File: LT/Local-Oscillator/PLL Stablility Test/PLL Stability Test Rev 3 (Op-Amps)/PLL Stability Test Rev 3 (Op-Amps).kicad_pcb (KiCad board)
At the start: 2 copper layers, 30 parts, among them J1 Conn_01x02_Male, J10 Conn_01x02_Male, J2 Conn_Coaxial, J3 Conn_01x02_Male, J4 Conn_01x02_Male, J5 Conn_Coaxial, J6 Conn_01x02_Male, J8 Conn_Coaxial, J9 Conn_01x03_Male, U1 LMH6611, U2 LMH6611

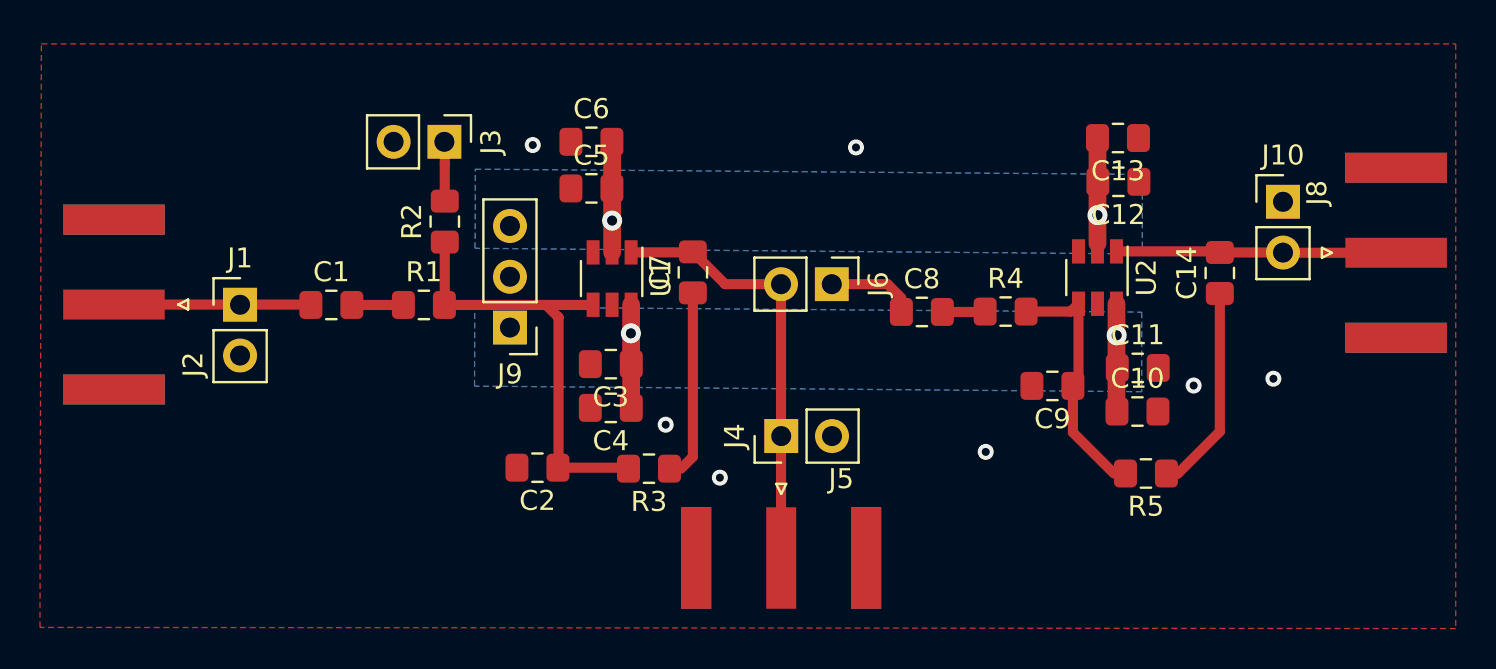
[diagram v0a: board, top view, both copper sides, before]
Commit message: Added the schematic for SE's flash memory board
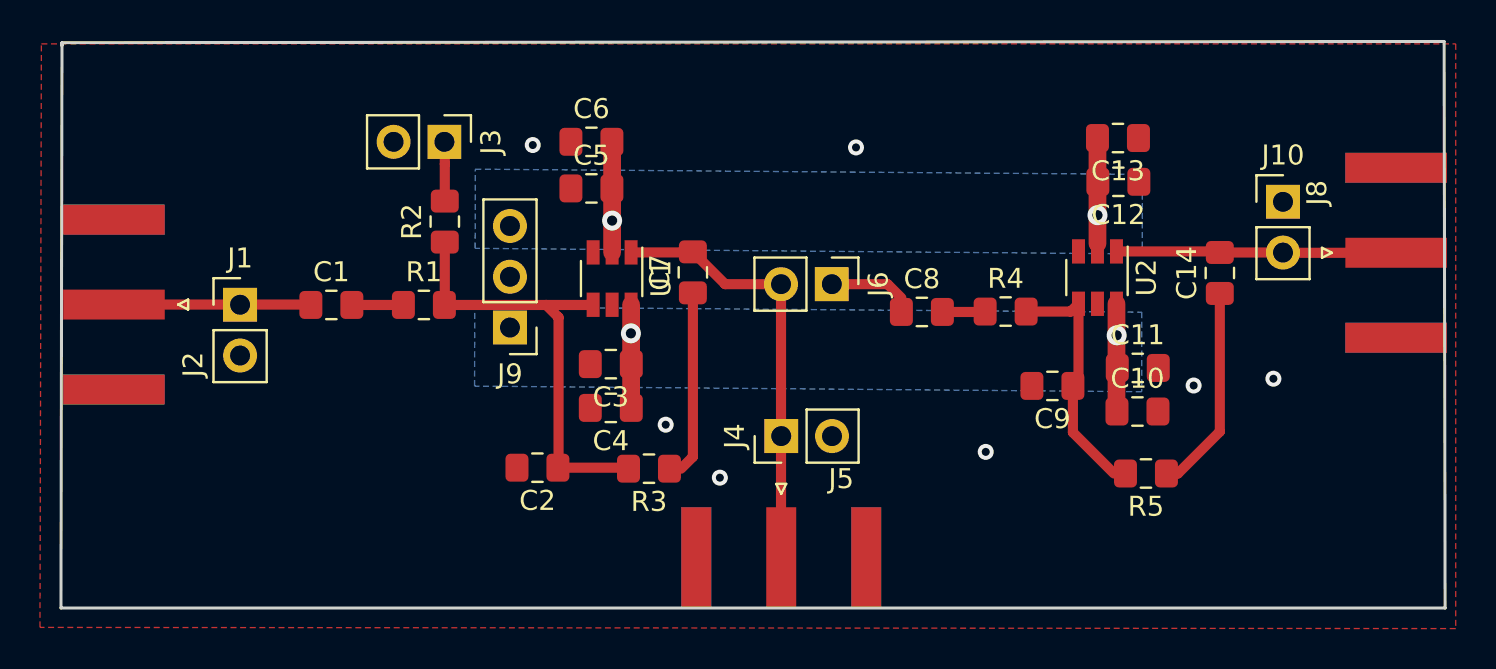
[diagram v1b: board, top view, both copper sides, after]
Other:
- board outline added: 69.2 x 28.3 mm
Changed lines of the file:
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@@
   (general
     (thickness 1.6)
-    (drawings 0)
+    (drawings 5)
     (tracks 64)
     (zones 0)
@@
       (drillshape 0)
       (scaleselection 1)
-      (outputdirectory "../../../../../../../../../../Volumes/USB30FD/Conner/PLL Op-Amp Test/"))
+      (outputdirectory "E:/Conner/PLL Op-Amp Test/Right_Here_Luis/"))
   )
   (net 0 "")
@@
     )
   )
+  (gr_line (start 38.16 16.84) (end 38.16 16.99) (layer Edge.Cuts) (width 0.15))
+  (gr_line (start 107.3 16.78) (end 38.16 16.84) (layer Edge.Cuts) (width 0.15))
+  (gr_line (start 107.35 45.12) (end 107.3 16.78) (layer Edge.Cuts) (width 0.15))
+  (gr_line (start 38.11 45.12) (end 107.35 45.12) (layer Edge.Cuts) (width 0.15))
+  (gr_line (start 38.16 16.88) (end 38.11 45.12) (layer Edge.Cuts) (width 0.15))
   (via (at 61.71 21.96) (size 0.8) (drill 0.4) (layers F.Cu B.Cu) (net 1))
   (via (at 77.88 22.08) (size 0.8) (drill 0.4) (layers F.Cu B.Cu) (net 1))
@@
   (via (at 90.92 31.48) (size 1.00076) (drill 0.508) (layers F.Cu B.Cu) (net 2))
   (via (at 66.62 31.38) (size 1.00076) (drill 0.508) (layers F.Cu B.Cu) (net 2))
-  (via (at 65.68 25.74) (size 1.00076) (drill 0.508) (layers F.Cu B.Cu) (net 3))
-  (via (at 89.96 25.47) (size 1.00076) (drill 0.508) (layers F.Cu B.Cu) (net 3))
   (segment (start 66.63 35.1) (end 66.64 35.11) (width 0.25) (layer F.Cu) (net 2) (status 30))
   (segment (start 66.63 29.95) (end 66.63 35.1) (width 0.889) (layer F.Cu) (net 2) (status 30))
   (segment (start 90.91 35.265) (end 90.935 35.29) (width 0.25) (layer F.Cu) (net 2))
   (segment (start 90.91 29.9) (end 90.91 35.265) (width 0.889) (layer F.Cu) (net 2))
+  (via (at 65.68 25.74) (size 1.00076) (drill 0.508) (layers F.Cu B.Cu) (net 3))
+  (via (at 89.96 25.47) (size 1.00076) (drill 0.508) (layers F.Cu B.Cu) (net 3))
   (segment (start 65.68 21.81) (end 65.67 21.8) (width 0.25) (layer F.Cu) (net 3) (status 30))
   (segment (start 65.68 27.33) (end 65.68 21.81) (width 0.889) (layer F.Cu) (net 3) (status 30))
@@
   (segment (start 50.59 29.94) (end 50.61 29.96) (width 0.25) (layer F.Cu) (net 5) (status 30))
   (segment (start 40.76 29.94) (end 50.59 29.94) (width 0.508) (layer F.Cu) (net 5) (status 30))
-  (segment (start 57.31 22.91) (end 57.31 24.765) (width 0.508) (layer F.Cu) (net 14) (status 20))
-  (segment (start 57.31 21.81) (end 57.31 22.91) (width 0.508) (layer F.Cu) (net 14) (status 10))
+  (segment (start 64.72 29.96) (end 64.73 29.95) (width 0.25) (layer F.Cu) (net 6) (status 30))
+  (segment (start 57.31 29.94) (end 57.29 29.96) (width 0.25) (layer F.Cu) (net 6) (status 30))
+  (segment (start 57.31 26.815) (end 57.31 29.94) (width 0.508) (layer F.Cu) (net 6) (status 30))
+  (segment (start 66.49 38.16) (end 66.5 38.15) (width 0.25) (layer F.Cu) (net 6))
+  (segment (start 63 30.58) (end 62.38 29.96) (width 0.508) (layer F.Cu) (net 6))
+  (segment (start 63 38.24) (end 63 30.58) (width 0.508) (layer F.Cu) (net 6))
+  (segment (start 57.29 29.96) (end 62.38 29.96) (width 0.508) (layer F.Cu) (net 6))
+  (segment (start 62.38 29.96) (end 64.72 29.96) (width 0.508) (layer F.Cu) (net 6))
+  (segment (start 66.45 38.1) (end 66.5 38.15) (width 0.25) (layer F.Cu) (net 6))
+  (segment (start 62.97 38.1) (end 66.45 38.1) (width 0.508) (layer F.Cu) (net 6))
   (segment (start 80.14 30.3) (end 80.15 30.31) (width 0.25) (layer F.Cu) (net 7) (status 30))
+  (segment (start 80.15 29.61) (end 80.15 30.31) (width 0.25) (layer F.Cu) (net 7))
+  (segment (start 79.46 28.92) (end 80.15 29.61) (width 0.508) (layer F.Cu) (net 7))
+  (segment (start 76.67 28.92) (end 79.46 28.92) (width 0.508) (layer F.Cu) (net 7))
   (segment (start 84.32 30.31) (end 84.34 30.29) (width 0.25) (layer F.Cu) (net 8) (status 30))
   (segment (start 82.2 30.31) (end 84.32 30.31) (width 0.508) (layer F.Cu) (net 8) (status 30))
@@
   (segment (start 69.695 27.33) (end 69.72 27.305) (width 0.25) (layer F.Cu) (net 11) (status 30))
   (segment (start 66.63 27.33) (end 69.695 27.33) (width 0.508) (layer F.Cu) (net 11) (status 30))
-  (segment (start 64.72 29.96) (end 64.73 29.95) (width 0.25) (layer F.Cu) (net 6) (status 30))
-  (segment (start 57.31 29.94) (end 57.29 29.96) (width 0.25) (layer F.Cu) (net 6) (status 30))
-  (segment (start 57.31 26.815) (end 57.31 29.94) (width 0.508) (layer F.Cu) (net 6) (status 30))
-  (segment (start 66.49 38.16) (end 66.5 38.15) (width 0.25) (layer F.Cu) (net 6))
-  (segment (start 63 30.58) (end 62.38 29.96) (width 0.508) (layer F.Cu) (net 6))
-  (segment (start 63 38.24) (end 63 30.58) (width 0.508) (layer F.Cu) (net 6))
-  (segment (start 57.29 29.96) (end 62.38 29.96) (width 0.508) (layer F.Cu) (net 6))
-  (segment (start 62.38 29.96) (end 64.72 29.96) (width 0.508) (layer F.Cu) (net 6))
-  (segment (start 66.45 38.1) (end 66.5 38.15) (width 0.25) (layer F.Cu) (net 6))
-  (segment (start 62.97 38.1) (end 66.45 38.1) (width 0.508) (layer F.Cu) (net 6))
-  (segment (start 80.15 29.61) (end 80.15 30.31) (width 0.25) (layer F.Cu) (net 7))
-  (segment (start 79.46 28.92) (end 80.15 29.61) (width 0.508) (layer F.Cu) (net 7))
-  (segment (start 76.67 28.92) (end 79.46 28.92) (width 0.508) (layer F.Cu) (net 7))
   (segment (start 71.335 28.92) (end 69.72 27.305) (width 0.508) (layer F.Cu) (net 11))
   (segment (start 74.13 28.92) (end 71.335 28.92) (width 0.508) (layer F.Cu) (net 11))
@@
   (segment (start 99.235 27.335) (end 99.24 27.34) (width 0.25) (layer F.Cu) (net 13))
   (segment (start 96.08 27.335) (end 99.235 27.335) (width 0.508) (layer F.Cu) (net 13))
+  (segment (start 57.31 22.91) (end 57.31 24.765) (width 0.508) (layer F.Cu) (net 14) (status 20))
+  (segment (start 57.31 21.81) (end 57.31 22.91) (width 0.508) (layer F.Cu) (net 14) (status 10))
   (zone (net 2) (net_name +5V) (layer B.Cu) (hatch edge 0.508)
     (connect_pads (clearance 0.508))
